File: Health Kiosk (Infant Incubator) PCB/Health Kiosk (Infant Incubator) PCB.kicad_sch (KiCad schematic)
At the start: 16 parts, among them J1 Jack-DC, J10 AD8232_Signals_to_IO_Expander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, J12 Circular_IP67_Connector_01x07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, J14 IO_Expansion_PowerIn_01x02_Pin, J15 I2C_Connector_to_IO_Expander_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, J2 RPI_IN_02x20_odd_even, J8 Sound_Analog_OUT_to_IO_Expand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, J9 AD8232_01x05_Socket, SW1 SW_Push

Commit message: pico and piconnections done. GPIOs pending
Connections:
- net 5V: now also A1.39 (VSYS), J2.4 (Pin_4)
- net GND: now also A1.13 (GND), A1.18 (GND), A1.23 (GND), A1.28 (GND), A1.3 (GND), A1.38 (GND), A1.8 (GND), J2.6 (Pin_6)
- net SCK: now also J2.3 (Pin_3)
- net SDA: now also J2.2 (Pin_2)
- net Tx: now reaches J2.14 (Pin_14)
- net Tx: now also A1.1 (GPIO0)
- net Rx: now reaches J2.15 (Pin_15)
- net Rx: now also A1.2 (GPIO1)

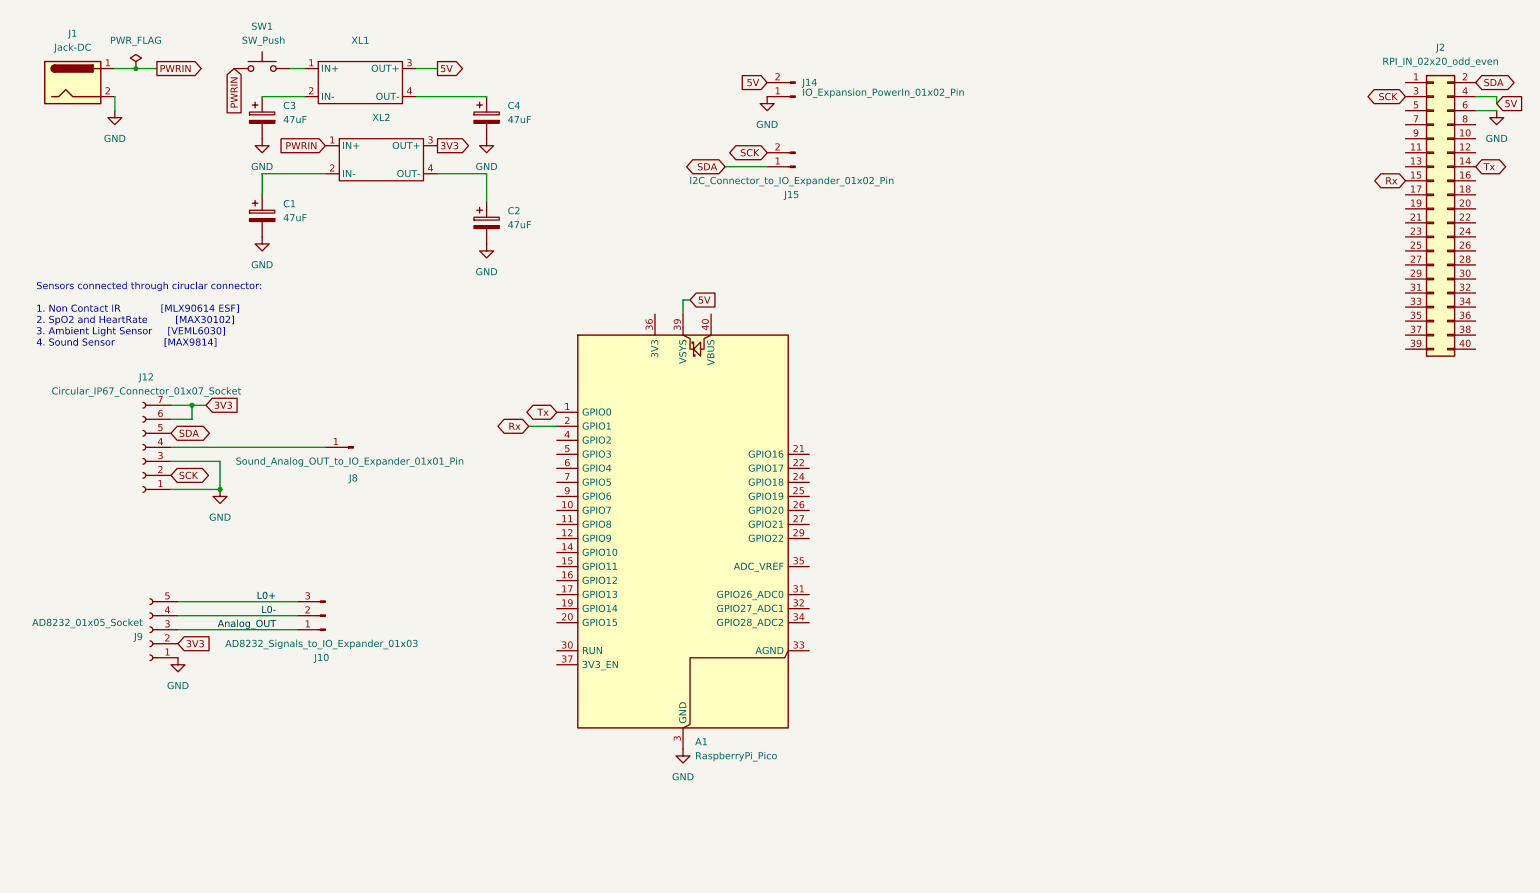
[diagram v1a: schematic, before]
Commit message: PCB Design Finished (Buck footprint left)
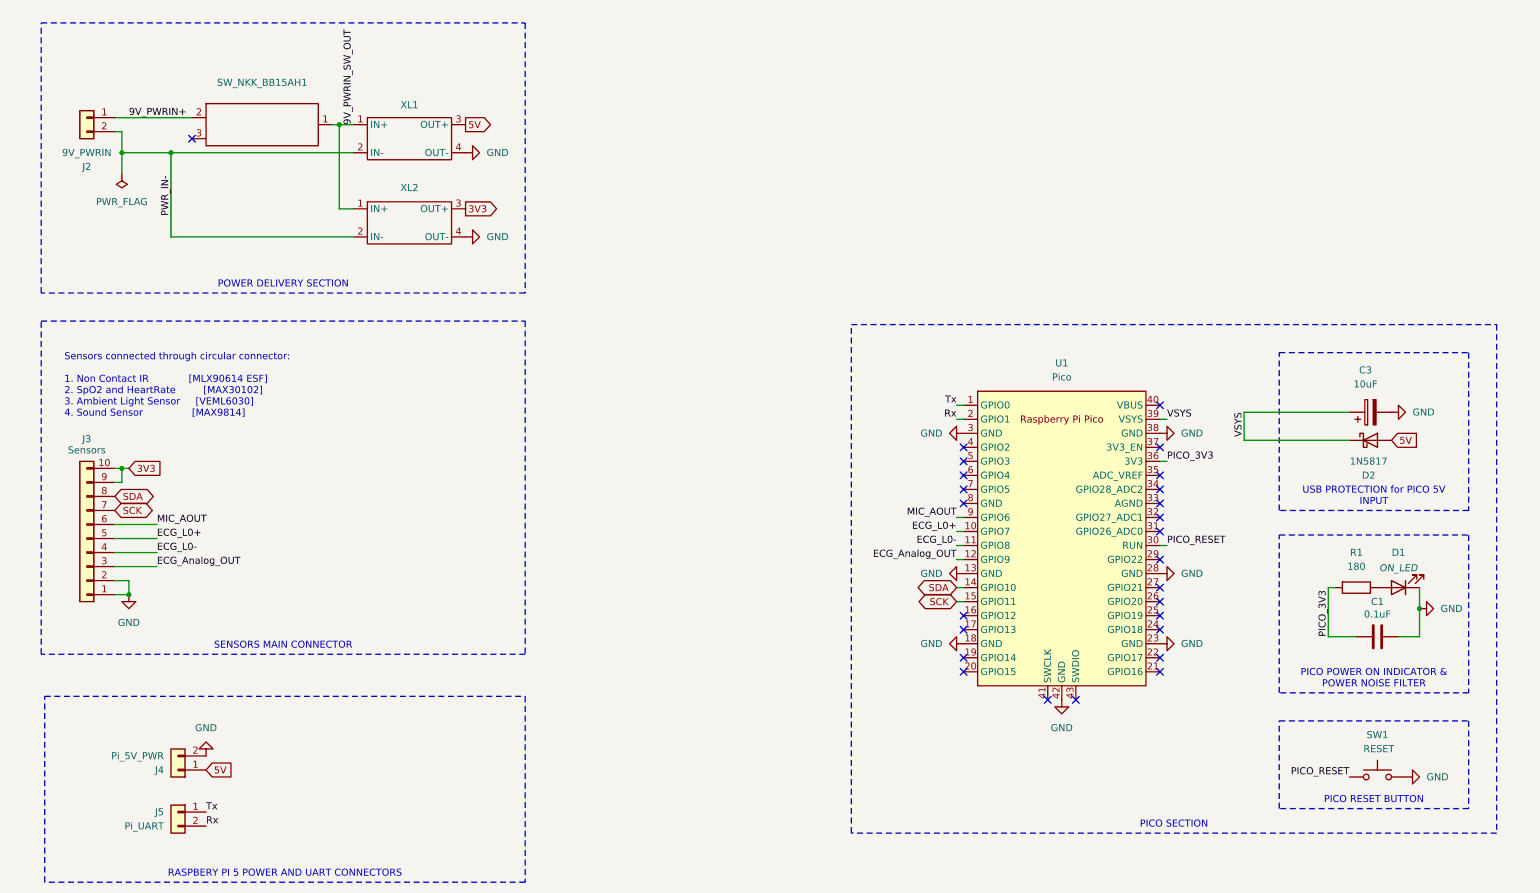
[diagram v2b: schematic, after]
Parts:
- removed A1: RaspberryPi_Pico, Module_RaspberryPi_Pico:RaspberryPi_Pico_Common, symbol MCU_Module_RaspberryPi_Pico:RaspberryPi_Pico
- removed C1, C2, C4: 47uF, symbol Device:C_Polarized
- removed J1: Jack-DC, symbol Connector:Jack-DC
- removed J10: AD8232_Signals_to_IO_Expander_01x03, symbol Connector:Conn_01x03_Pin
- removed J12: Circular_IP67_Connector_01x07_Socket, Connector_Harwin:Harwin_M20-89007xx_1x07_P2.54mm_Horizontal, symbol Connector:Conn_01x07_Socket
- removed J14: IO_Expansion_PowerIn_01x02_Pin, Connector_JST:JST_XH_B2B-XH-A_1x02_P2.50mm_Vertical, symbol Connector:Conn_01x02_Pin
- removed J15: I2C_Connector_to_IO_Expander_01x02_Pin, Connector_JST:JST_XH_B2B-XH-AM_1x02_P2.50mm_Vertical, symbol Connector:Conn_01x02_Pin
- removed J2: RPI_IN_02x20_odd_even, Connector_PinHeader_2.54mm:PinHeader_2x20_P2.54mm_Horizontal, symbol Connector_Generic:Conn_02x20_Odd_Even
- removed J8: Sound_Analog_OUT_to_IO_Expander_01x01_Pin, symbol Connector:Conn_01x01_Pin
- removed J9: AD8232_01x05_Socket, symbol Connector:Conn_01x05_Socket
- added C1: 0.1uF, Capacitor_THT:C_Disc_D10.5mm_W5.0mm_P5.00mm, symbol Device:C
- added D1: ON_LED, LED_THT:LED_Rectangular_W5.0mm_H2.0mm_Horizontal_O1.27mm_Z1.0mm, symbol Device:LED
- added D2: 1N5817, Diode_THT:D_DO-41_SOD81_P10.16mm_Horizontal, symbol Diode:1N5817
- added J2: 9V_PWRIN, Connector_JST:JST_XH_S2B-XH-A-1_1x02_P2.50mm_Horizontal, symbol Connector_Generic:Conn_01x02
- added J3: Sensors, Connector_JST:JST_XH_S10B-XH-A-1_1x10_P2.50mm_Horizontal, symbol Connector_Generic:Conn_01x10
- added J4: Pi_5V_PWR, Connector_JST:JST_XH_S2B-XH-A-1_1x02_P2.50mm_Horizontal, symbol Connector_Generic:Conn_01x02
- added J5: Pi_UART, Connector_JST:JST_XH_S2B-XH-A-1_1x02_P2.50mm_Horizontal, symbol Connector_Generic:Conn_01x02
- added R1: 180, Resistor_THT:R_Axial_DIN0207_L6.3mm_D2.5mm_P7.62mm_Horizontal, symbol Device:R
- added SW_NKK_BB15AH1: ~, Button_Switch_THT:SW_NKK_BB15AH, symbol SW_NKK_BB15AH:Switch_Rugged
- added U1: Pico, MCU_RaspberryPi_and_Boards:RPi_Pico_SMD_TH, symbol MCU_RaspberryPi_and_Boards:Pico
- C3: value 47uF -> 10uF; footprint (none) -> Capacitor_THT:CP_Radial_D5.0mm_P2.50mm
- SW1: value SW_Push -> RESET
- XL1, XL2: footprint (none) -> DC_DC_Converter:XL4015
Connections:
- net 3V3: now also J3.10 (Pin_10), J3.9 (Pin_9)
- net 5V: now also D2.2 (A), J4.1 (Pin_1)
- net GND: now also SW1.2, XL1.4 (OUT-), XL2.4 (OUT-), C1.2, D1.1 (K), J3.1 (Pin_1), J3.2 (Pin_2), J4.2 (Pin_2), U1.13 (GND), U1.18 (GND), U1.23 (GND), U1.28 (GND), U1.3 (GND), U1.38 (GND), U1.42 (GND)
- net Rx: now also J5.2 (Pin_2), U1.2 (GPIO1)
- net SCK: now also J3.7 (Pin_7), U1.15 (GPIO11)
- net SDA: now also J3.8 (Pin_8), U1.14 (GPIO10)
- net Tx: now also J5.1 (Pin_1), U1.1 (GPIO0)
- net PWR_IN-: now reaches XL2.2 (IN-)
- net PWR_IN-: now also XL1.2 (IN-), J2.2 (Pin_2)
- net 9V_PWRIN_SW_OUT: now reaches XL1.1 (IN+)
- net 9V_PWRIN_SW_OUT: now also XL2.1 (IN+), SW_NKK_BB15AH1.1; no longer SW1.2
- net VSYS: now reaches C3.1
- net VSYS: now also D2.1 (K), U1.39 (VSYS); no longer XL1.2 (IN-)
- net PWRIN renamed PICO_RESET
- net PICO_RESET: now also U1.30 (RUN); no longer XL2.1 (IN+)
- new net: D1.2 (A), R1.1
- new net 9V_PWRIN+: J2.1 (Pin_1), SW_NKK_BB15AH1.2
- new net ECG_Analog_OUT: J3.3 (Pin_3), U1.12 (GPIO9)
- new net ECG_L0+: J3.5 (Pin_5), U1.10 (GPIO7)
- new net ECG_L0-: J3.4 (Pin_4), U1.11 (GPIO8)
- new net MIC_AOUT: J3.6 (Pin_6), U1.9 (GPIO6)
- new net PICO_3V3: C1.1, R1.2, U1.36 (3V3)
- no-connect marks 0 -> 26
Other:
- note added: "Sensors connected through circular connector: 1. Non Contact IR [MLX90614 ESF] 2. SpO2 and HeartRate [MAX30102] 3. Ambient Light Sensor [VEML6030] 4. Sound Sensor [MAX9814]"
- note removed: "Sensors connected through ciruclar connector: 1. Non Contact IR [MLX90614 ESF] 2. SpO2 and HeartRate [MAX30102] 3. Ambient Light Sensor [VEML6030] 4. Sound Sensor [MAX9814]"
- title: (none) -> NeoCocoon
- moved on the sheet: SW1, XL1, XL2
